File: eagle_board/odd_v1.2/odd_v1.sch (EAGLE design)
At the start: 25 parts

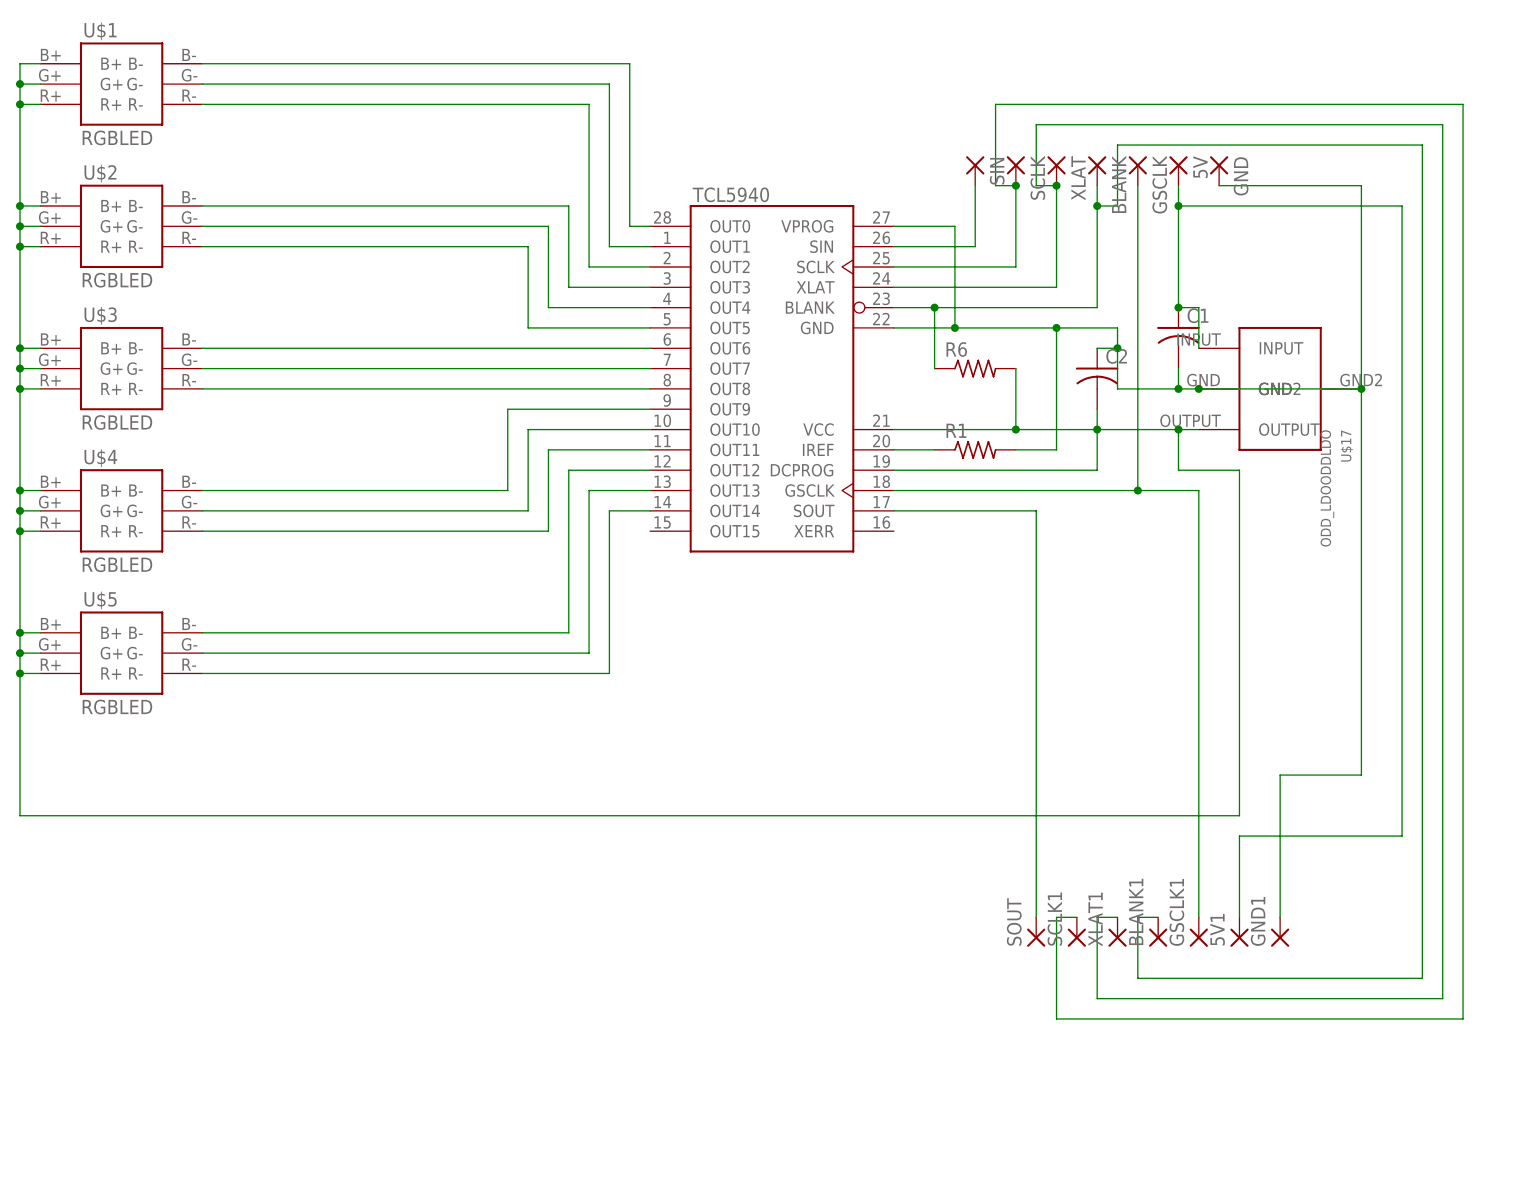
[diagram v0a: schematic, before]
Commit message: Moved around components on the board to make some paths shorter
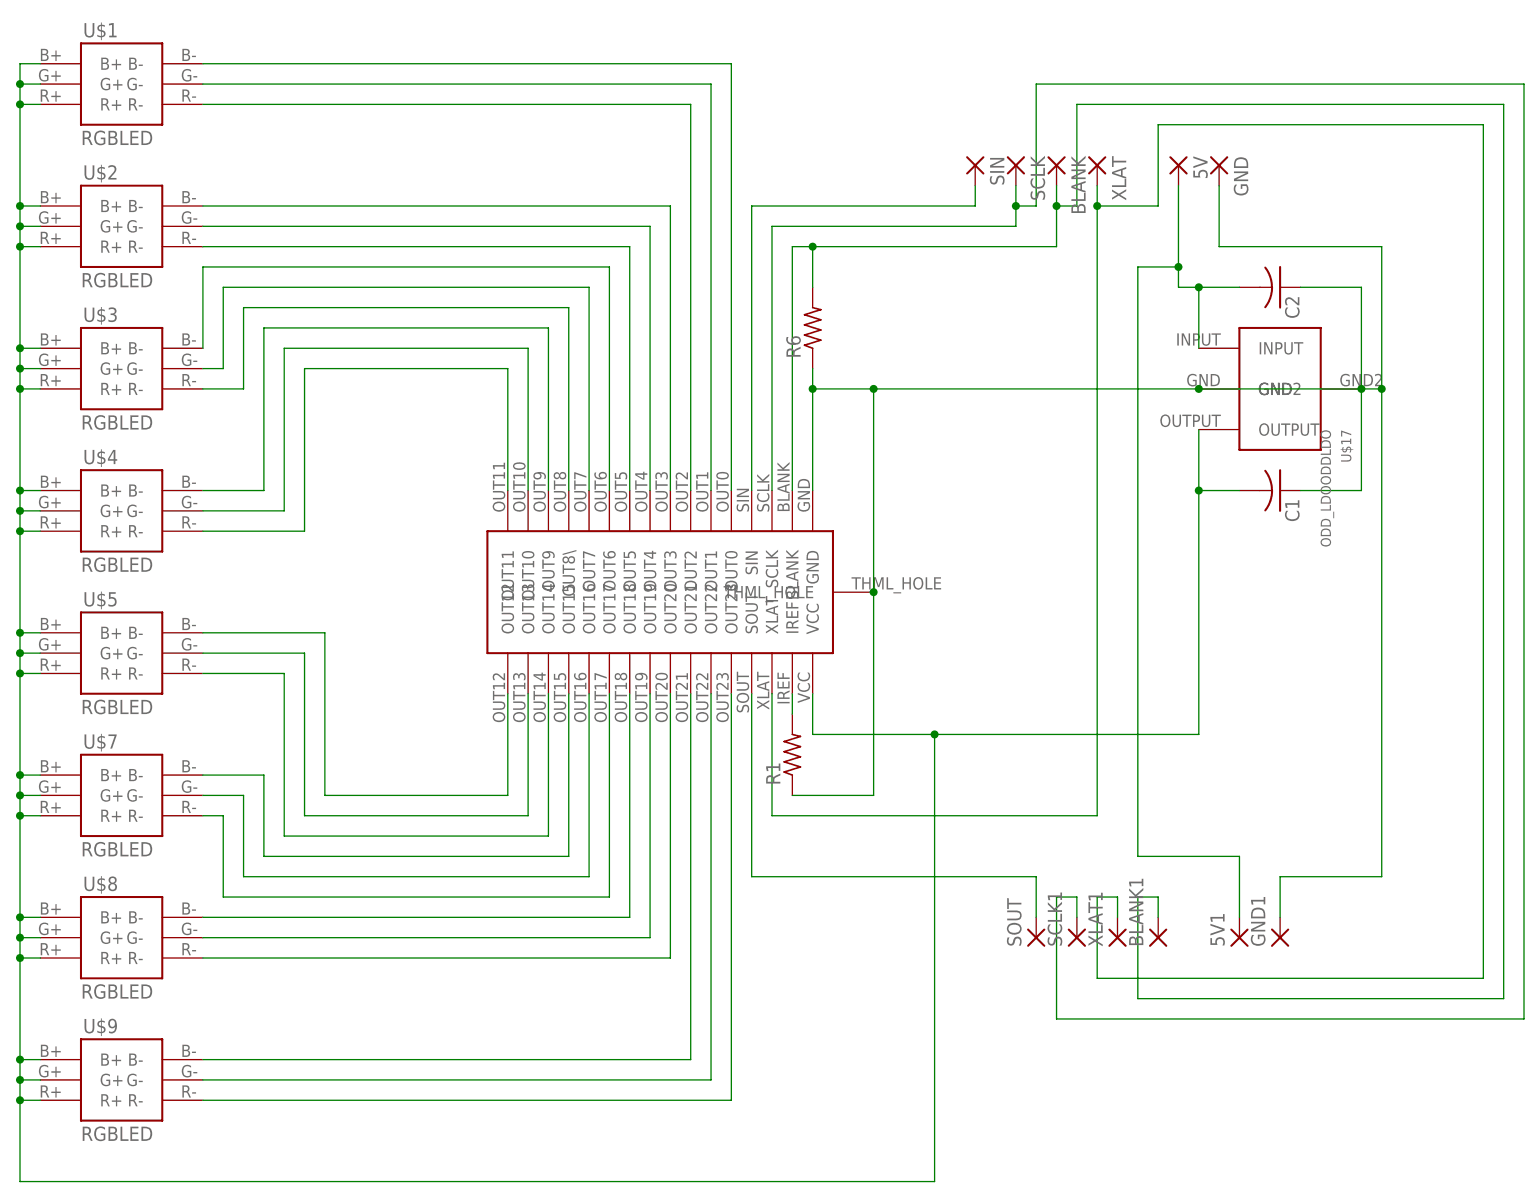
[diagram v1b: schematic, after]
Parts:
- removed GSCLK, GSCLK1: (no value), wirepad:2,54/1,1
- removed IC1: (no value), tcl5940:TCL5940
- added U$6: TLC5947, tlc5947:TLC5947
- added U$7, U$8, U$9: RGBLED, odd_led:CREESMDRGBLED6PADSMD
- C1, C2: device resistor:C-US075-032X103 -> resistor:C-US050-025X075
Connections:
- removed net N$1: IC1.OUT0, U$1.B-
- removed net N$50: IC1.SOUT, SOUT.P
- removed net N$54: BLANK.P, BLANK1.P, IC1.BLANK, R6.1
- removed net N$58: IC1.IREF, R1.1
- new net N$23: U$3.R-, U$6.OUT8\
- new net N$24: U$4.B-, U$6.OUT9
- new net N$25: U$4.G-, U$6.OUT10
- new net N$26: U$4.R-, U$6.OUT11
- new net N$27: C1.2, U$1.B+, U$1.G+, U$1.R+, U$17.OUTPUT, U$2.B+, U$2.G+, U$2.R+, U$3.B+, U$3.G+, U$3.R+, U$4.B+, U$4.G+, U$4.R+, U$5.B+, U$5.G+, U$5.R+, U$6.VCC, U$7.B+, U$7.G+, U$7.R+, U$8.B+, U$8.G+, U$8.R+, U$9.B+, U$9.G+, U$9.R+
- new net N$28: 5V.P, 5V1.P, C2.2, U$17.INPUT
- new net N$29: SIN.P, U$6.SIN
- new net N$30: SCLK.P, SCLK1.P, U$6.SCLK
- new net N$32: R1.2, U$6.IREF
- new net N$33: BLANK.P, BLANK1.P, R6.2, U$6.BLANK
- new net N$34: C1.1, C2.1, GND.P, GND1.P, R1.1, R6.1, U$17.GND, U$17.GND2, U$6.GND, U$6.THML_HOLE
- new net N$35: SOUT.P, U$6.SOUT
- net N$10: now also U$6.OUT18, U$8.B-; no longer IC1.SIN, SIN.P
- net N$11: now also U$6.OUT17, U$7.R-; no longer IC1.OUT14, U$5.R-
- net N$12: now also U$6.OUT16, U$7.G-; no longer IC1.OUT13, U$5.G-
- net N$13: now also U$6.OUT15, U$7.B-; no longer IC1.OUT12, U$5.B-
- net N$14: now also U$5.R-, U$6.OUT14; no longer IC1.OUT11, U$4.R-
- net N$15: now also U$5.G-, U$6.OUT13; no longer IC1.OUT10, U$4.G-
- net N$16: now also U$5.B-, U$6.OUT12; no longer IC1.OUT9, U$4.B-
- net N$17: now also U$2.B-, U$6.OUT3; no longer IC1.SCLK, SCLK.P, SCLK1.P
- net N$18: now also U$6.XLAT, XLAT.P, XLAT1.P; no longer 5V.P, 5V1.P, C1.1, U$17.INPUT
- net N$19: now also U$2.G-, U$6.OUT4; no longer C1.2, C2.1, GND.P, GND1.P, IC1.GND, IC1.VPROG, R1.2, U$17.GND, U$17.GND2
- net N$2: now also U$1.B-, U$6.OUT0; no longer IC1.OUT1, U$1.G-
- net N$20: now also U$2.R-, U$6.OUT5; no longer IC1.XLAT, XLAT.P, XLAT1.P
- net N$21: now also U$3.B-, U$6.OUT6; no longer GSCLK.P, GSCLK1.P, IC1.GSCLK
- net N$22: now also U$3.G-, U$6.OUT7; no longer C2.2, IC1.DCPROG, IC1.VCC, R6.2, U$1.B+, U$1.G+, U$1.R+, U$17.OUTPUT, U$2.B+, U$2.G+, U$2.R+, U$3.B+, U$3.G+, U$3.R+, U$4.B+, U$4.G+, U$4.R+, U$5.B+, U$5.G+, U$5.R+
- net N$3: now also U$1.G-, U$6.OUT1; no longer IC1.OUT2, U$1.R-
- net N$4: now also U$1.R-, U$6.OUT2; no longer IC1.OUT3, U$2.B-
- net N$5: now also U$6.OUT23, U$9.R-; no longer IC1.OUT4, U$2.G-
- net N$6: now also U$6.OUT22, U$9.G-; no longer IC1.OUT5, U$2.R-
- net N$7: now also U$6.OUT21, U$9.B-; no longer IC1.OUT6, U$3.B-
- net N$8: now also U$6.OUT20, U$8.R-; no longer IC1.OUT7, U$3.G-
- net N$9: now also U$6.OUT19, U$8.G-; no longer IC1.OUT8, U$3.R-
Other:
- moved on the sheet: BLANK, C1, C2, R1, R6, XLAT
